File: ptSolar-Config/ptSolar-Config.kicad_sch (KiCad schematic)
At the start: 12 parts, among them J1 6 Pin Male Header, J2 Programming, J3 USB_B_Micro, SW1 Reset Switch, U1 CH340X

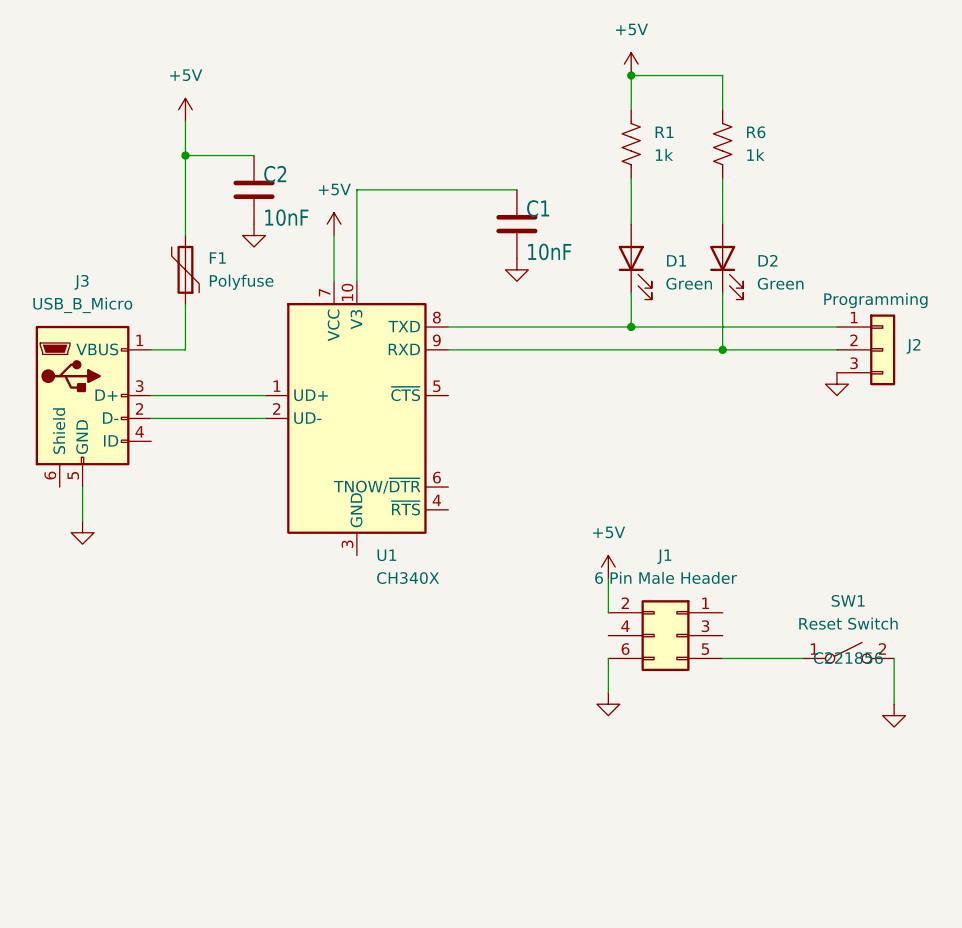
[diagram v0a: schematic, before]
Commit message: Updated to firmware 1.0.1
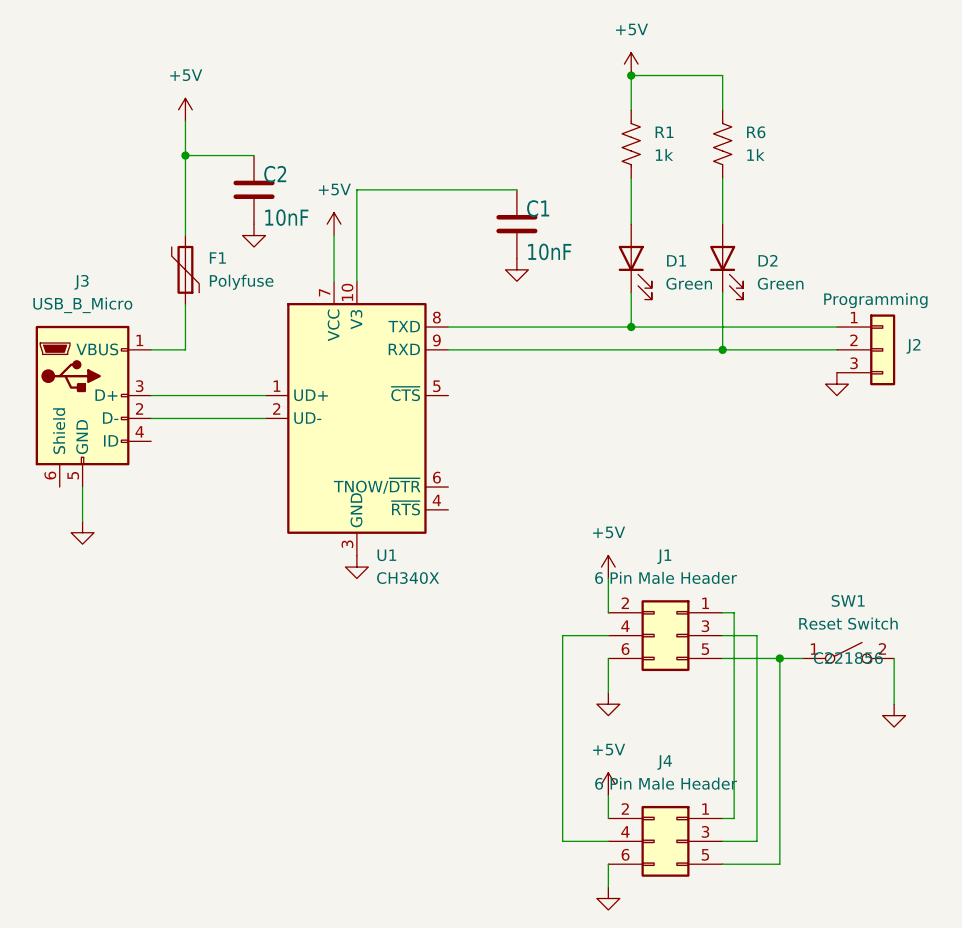
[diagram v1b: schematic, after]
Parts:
- added J4: 6 Pin Male Header, Connector_PinHeader_2.54mm:PinHeader_2x03_P2.54mm_Vertical, symbol Connector_Generic:Conn_02x03_Odd_Even
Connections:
- net +5V: now also J4.2 (Pin_2)
- net GND: now also U1.3 (GND), J4.6 (Pin_6)
- net at J1.1 (Pin_1): now also J4.1 (Pin_1)
- net at J1.3 (Pin_3): now also J4.3 (Pin_3)
- net at J1.4 (Pin_4): now also J4.4 (Pin_4)
- net at J1.5 (Pin_5), SW1.1 (A): now also J4.5 (Pin_5)
